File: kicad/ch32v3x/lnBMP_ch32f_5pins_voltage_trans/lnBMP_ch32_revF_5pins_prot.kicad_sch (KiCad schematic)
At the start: 25 parts, among them J1 Conn_ARM_JTAG_SWD_10, J3 Debug port, J4 USB_C_Receptacle, J5 Debug port, U1 CH32V303RCT6, U2 LM1117-3.3, Y1 Crystal

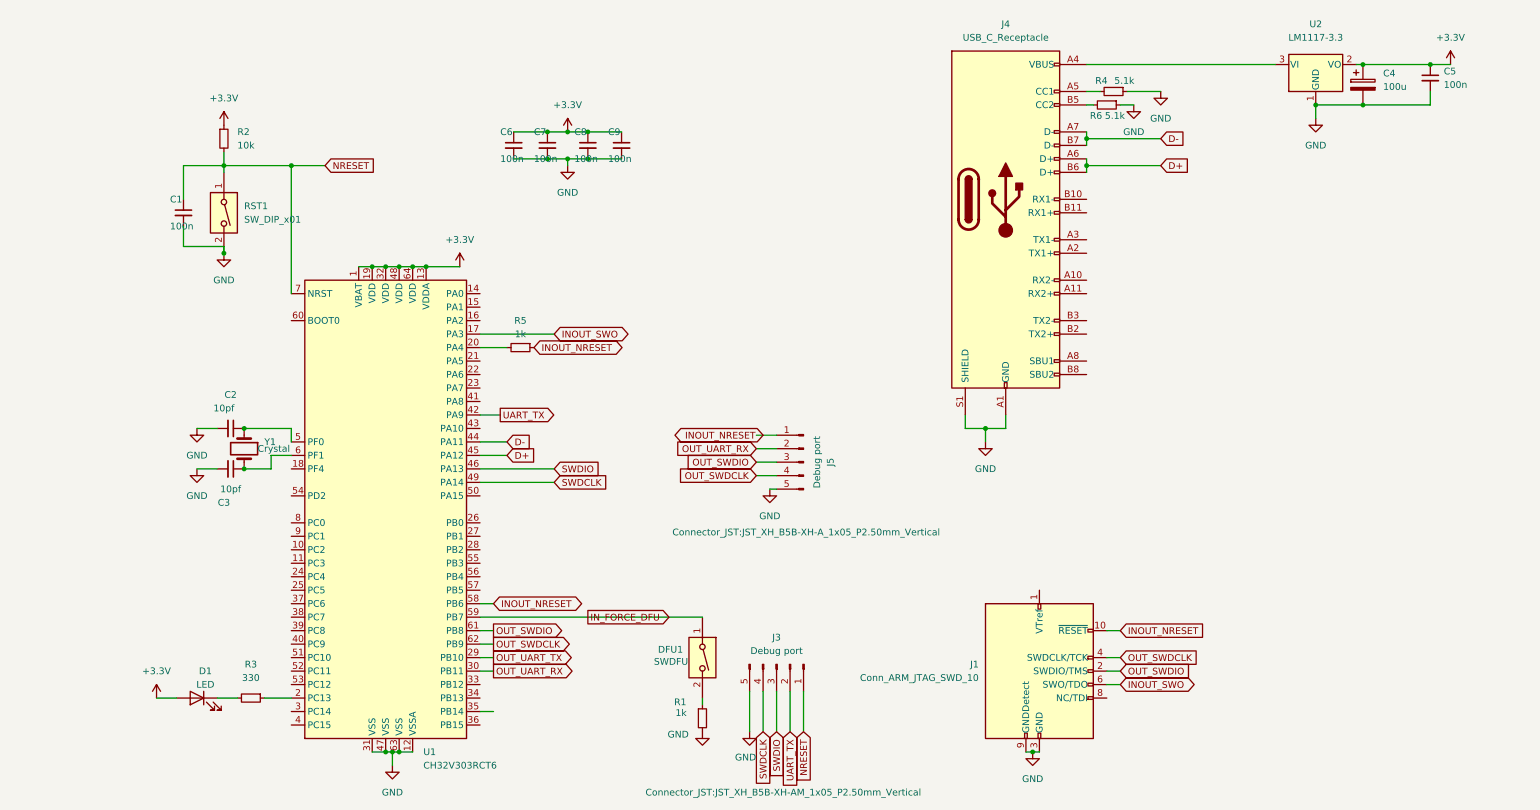
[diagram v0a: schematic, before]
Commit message: add level shifter
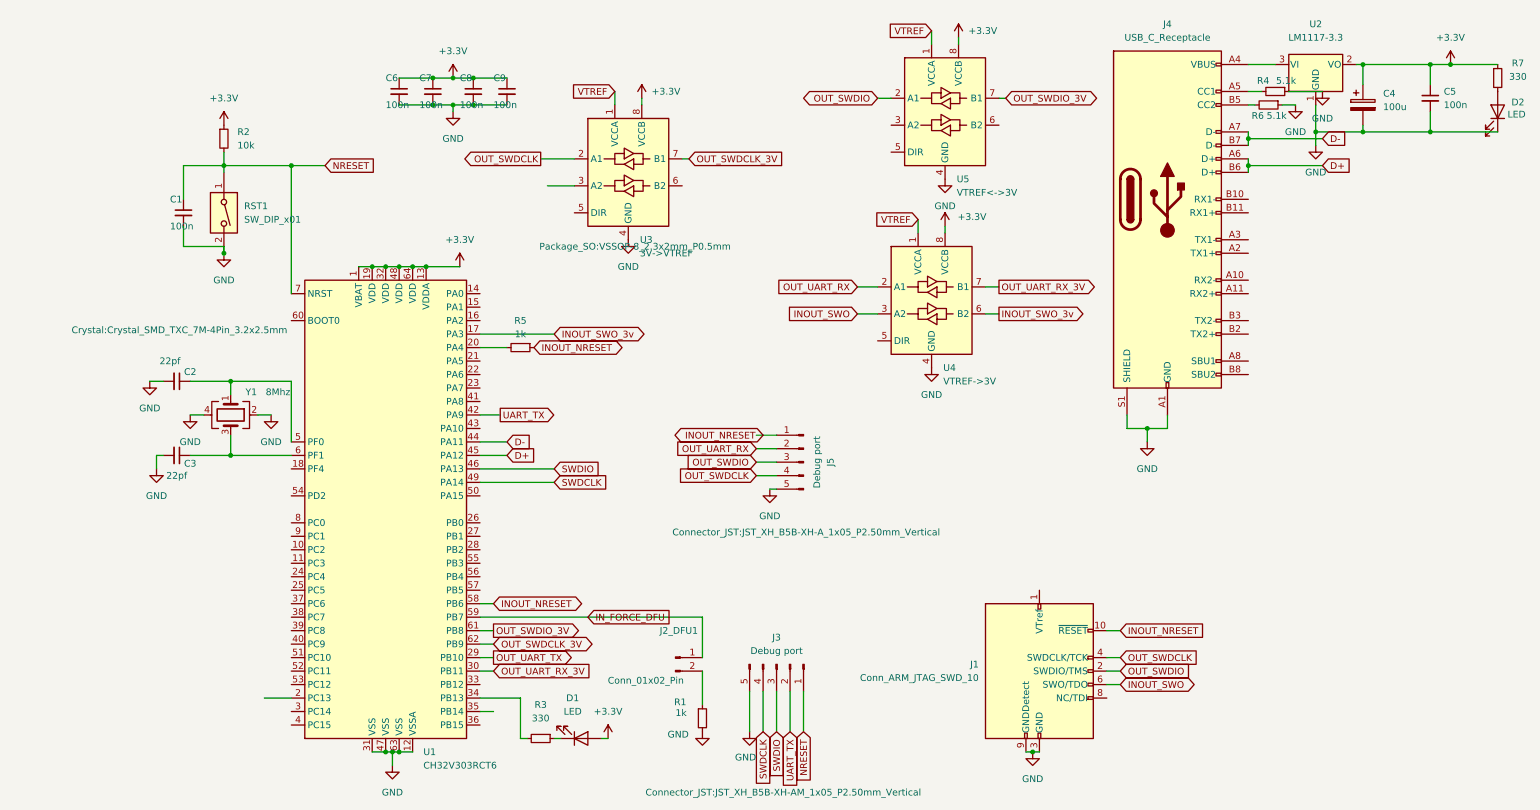
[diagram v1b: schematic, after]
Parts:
- removed DFU1: SWDFU, Button_Switch_SMD:SW_SPST_CK_RS282G05A3, symbol Switch:SW_DIP_x01
- removed Y1: Crystal, Crystal:Crystal_HC49-U_Vertical, symbol Device:Crystal
- added D2: LED, Diode_SMD:D_0805_2012Metric, symbol Device:LED
- added J2_DFU1: Conn_01x02_Pin, Connector_PinHeader_1.27mm:PinHeader_1x02_P1.27mm_Vertical, symbol Connector:Conn_01x02_Pin
- added R7: 330, Resistor_SMD:R_0603_1608Metric, symbol Device:R_Small
- added U3: 3V->VTREF, Package_SO:VSSOP-8_2.3x2mm_P0.5mm, symbol Logic_LevelTranslator:SN74LVC2T45DCUR
- added U4: VTREF->3V, Package_SO:VSSOP-8_2.3x2mm_P0.5mm, symbol Logic_LevelTranslator:SN74LVC2T45DCUR
- added U5: VTREF<->3V, Package_SO:VSSOP-8_2.3x2mm_P0.5mm, symbol Logic_LevelTranslator:SN74LVC2T45DCUR
- added Y1: 8Mhz, Crystal:Crystal_SMD_TXC_7M-4Pin_3.2x2.5mm, symbol Device:Crystal_GND24
- C2, C3: value 10pf -> 22pf
- C4: footprint Capacitor_THT:CP_Radial_D4.0mm_P2.00mm -> Capacitor_SMD:C_1206_3216Metric_Pad1.33x1.80mm_HandSolder
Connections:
- net +3.3V: now also R7.1, U3.8 (VCCB), U4.8 (VCCB), U5.8 (VCCB)
- net GND: now also D2.1 (K), U3.4 (GND), U4.4 (GND), U5.4 (GND), Y1.2, Y1.4
- net INOUT_SWO: now also U4.3 (A2); no longer U1.17 (PA3)
- net IN_FORCE_DFU: now also J2_DFU1.1 (Pin_1)
- net OUT_SWDCLK: now also U3.2 (A1); no longer U1.62 (PB9)
- net OUT_SWDIO: now also U5.2 (A1); no longer U1.61 (PB8)
- net OUT_UART_RX: now also U4.2 (A1); no longer U1.30 (PB11)
- net at C3.1, U1.6 (PF1): now also Y1.3
- net at R1.1: now also J2_DFU1.2 (Pin_2)
- net at D1.1 (K): now also R3.1; no longer R3.2
- net at U1.2 (PC13): no longer R3.1
- net at U1.34 (PB13): now also R3.2
- net at C2.1, U1.5 (PF0): now also Y1.1
- new net: D2.2 (A), R7.2
- new net INOUT_SWO_3v: U1.17 (PA3), U4.6 (B2)
- new net OUT_SWDCLK_3V: U1.62 (PB9), U3.7 (B1)
- new net OUT_SWDIO_3V: U1.61 (PB8), U5.7 (B1)
- new net OUT_UART_RX_3V: U1.30 (PB11), U4.7 (B1)
- new net VTREF: U3.1 (VCCA), U4.1 (VCCA), U5.1 (VCCA)
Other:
- moved on the sheet: C2, C3, C4, C5, C6, C7, C8, C9, D1, J4, R3, R4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

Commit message: CH32:; add voltage shifter  (cont)
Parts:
- added C10, C11: 100n, Resistor_SMD:R_0603_1608Metric, symbol Device:C_Small
- added J2: Conn_01x03_Socket, Connector_PinHeader_1.27mm:PinHeader_1x03_P1.27mm_Vertical, symbol Connector:Conn_01x03_Socket
- added U6: RT9013-33GB, PCM_Package_TO_SOT_SMD_AKL:TSOT-23-5, symbol 2024-10-20_09-04-45:RT9013-33GB
- J1: value Conn_ARM_JTAG_SWD_10 -> jtag
- J2_DFU1: value Conn_01x02_Pin -> con2
- J3: value Debug port -> Dbg; footprint Connector_JST:JST_XH_B5B-XH-AM_1x05_P2.50mm_Vertical -> con5
- J4: value USB_C_Receptacle -> USB
- J5: footprint Connector_JST:JST_XH_B5B-XH-A_1x05_P2.50mm_Vertical -> Con5
- U3: footprint Package_SO:VSSOP-8_2.3x2mm_P0.5mm -> Voltshif
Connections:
- net +3.3V: now also U5.1 (VCCA), C10.1, J2.1 (Pin_1), U6.1 (VIN), U6.3 (EN); no longer U5.8 (VCCB)
- net GND: now also U3.5 (DIR), C10.2, C11.2, U6.2 (GND)
- net OUT_SWDIO: now also U5.7 (B1); no longer U5.2 (A1)
- net OUT_SWDIO_3V: now also U5.2 (A1); no longer U5.7 (B1)
- net VTREF: now also U4.5 (DIR), U5.8 (VCCB), J2.2 (Pin_2); no longer U5.1 (VCCA)
- net SWIO_DIR_3V: now reaches U5.5 (DIR)
- net SWIO_DIR_3V: now also U1.3 (PC14)
- new net V1.8: C11.1, J2.3 (Pin_3), U6.5 (VOUT)
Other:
- title: (none) -> Swindle CH32V303

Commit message: kicad: update to correct voltage translator footprint
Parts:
- J3: footprint con5 -> Connector_JST:JST_XH_B5B-XH-A_1x05_P2.50mm_Vertical
- J5: footprint Con5 -> Connector_JST:JST_XH_B5B-XH-A_1x05_P2.50mm_Vertical
- U3: footprint Voltshif -> Package_SO:TSSOP-8_3x3mm_P0.65mm
- U4, U5: footprint Package_SO:VSSOP-8_2.3x2mm_P0.5mm -> Package_SO:TSSOP-8_3x3mm_P0.65mm
- Y1: footprint Crystal:Crystal_SMD_TXC_7M-4Pin_3.2x2.5mm -> footprints:Crystal_SMD_TXC_7M-4Pin_3.2x2.5mm_45deg
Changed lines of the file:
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@@
 			)
 		)
-		(property "Footprint" "Con5"
+		(property "Footprint" "Connector_JST:JST_XH_B5B-XH-A_1x05_P2.50mm_Vertical"
 			(at 147.828 112.268 0)
 			(effects
@@
 			)
 		)
-		(property "Footprint" "Package_SO:VSSOP-8_2.3x2mm_P0.5mm"
+		(property "Footprint" "Package_SO:TSSOP-8_3x3mm_P0.65mm"
 			(at 175.26 46.99 0)
 			(effects
@@
 			)
 		)
-		(property "Footprint" "Voltshif"
+		(property "Footprint" "Package_SO:TSSOP-8_3x3mm_P0.65mm"
 			(at 118.364 23.622 0)
 			(effects
@@
 			)
 		)
-		(property "Footprint" "Package_SO:VSSOP-8_2.3x2mm_P0.5mm"
+		(property "Footprint" "Package_SO:TSSOP-8_3x3mm_P0.65mm"
 			(at 172.72 82.55 0)
 			(effects
@@
 			)
 		)
-		(property "Footprint" "con5"
+		(property "Footprint" "Connector_JST:JST_XH_B5B-XH-A_1x05_P2.50mm_Vertical"
 			(at 143.51 161.29 90)
 			(effects
@@
 			)
 		)
-		(property "Footprint" "Crystal:Crystal_SMD_TXC_7M-4Pin_3.2x2.5mm"
+		(property "Footprint" "footprints:Crystal_SMD_TXC_7M-4Pin_3.2x2.5mm_45deg"
 			(at 29.718 74.168 90)
 			(effects
